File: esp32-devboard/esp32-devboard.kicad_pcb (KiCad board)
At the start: 2 copper layers, 79.4 x 40.6 mm, 33 parts, among them J1 Conn_01x40, J10 Conn_01x02, J11 Conn_01x02, J12 TPS2065DBVR, J13 Conn_01x01, J14 Conn_01x01, J2 Conn_01x40, J3 USB_B_Micro, J4 RJ12, J5 Barrel_Jack_Switch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

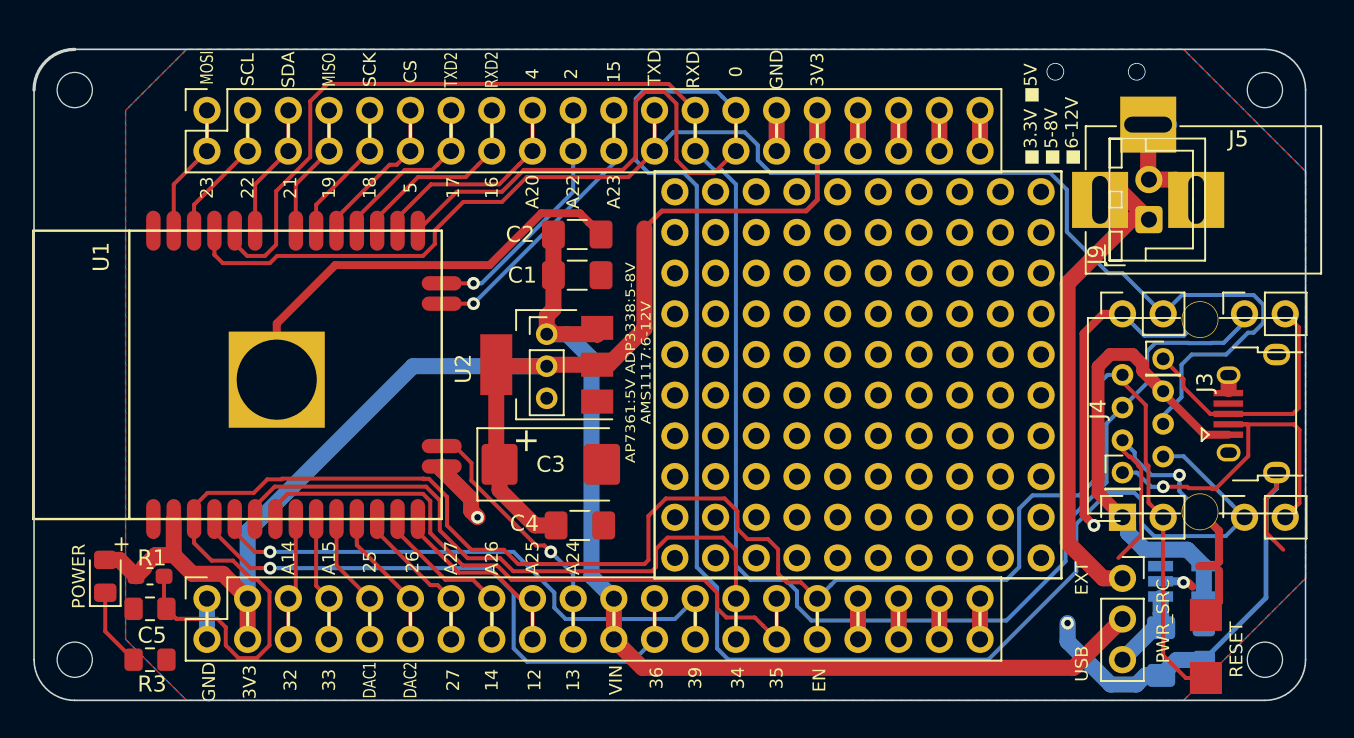
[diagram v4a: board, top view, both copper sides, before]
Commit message: add/enlarge holes
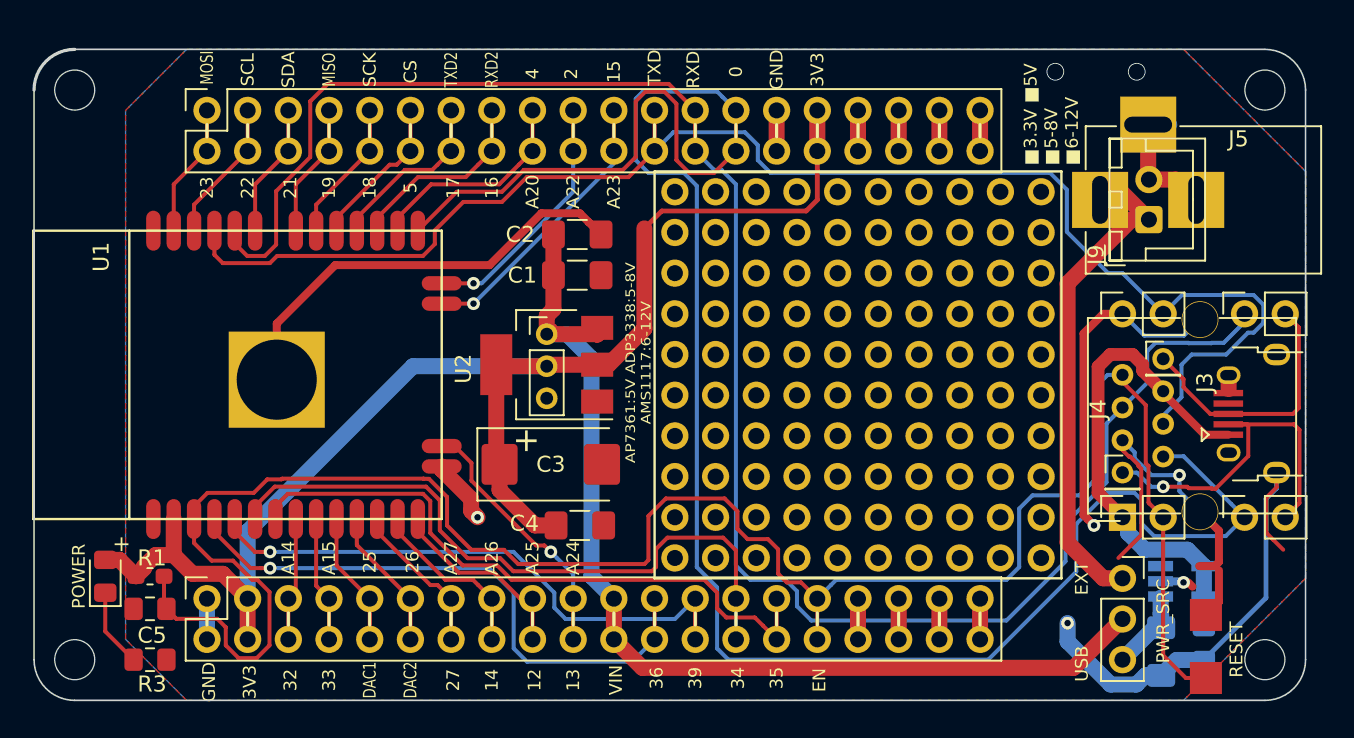
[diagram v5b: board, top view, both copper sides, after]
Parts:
- REF** (x4): value MountingHole_2.2mm_M2 -> MountingHole_2.5mm; footprint MountingHole:MountingHole_2.2mm_M2 -> MountingHole:MountingHole_2.5mm
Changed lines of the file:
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@@
     (add_net GND)
+  )
+  (module MountingHole:MountingHole_2.5mm (layer F.Cu)
+    (at 118.745 110.49)
+    (descr "Mounting Hole 2.5mm, no annular")
+    (tags "mounting hole 2.5mm no annular")
+    (attr virtual)
+    (fp_text reference REF** (at 0 -3.5) (layer F.SilkS) hide
+      (effects (font (size 1 1) (thickness 0.15)))
+    )
+    (fp_text value MountingHole_2.5mm (at 0 3.5) (layer F.Fab)
+      (effects (font (size 1 1) (thickness 0.15)))
+    )
+    (fp_circle (center 0 0) (end 2.75 0) (layer F.CrtYd) (width 0.05))
+    (fp_circle (center 0 0) (end 2.5 0) (layer Cmts.User) (width 0.15))
+    (fp_text user %R (at 0.3 0) (layer F.Fab)
+      (effects (font (size 1 1) (thickness 0.15)))
+    )
+    (pad 1 np_thru_hole circle (at 0 0) (size 2.5 2.5) (drill 2.5) (layers *.Cu *.Mask))
+  )
+  (module MountingHole:MountingHole_2.5mm (layer F.Cu)
+    (at 118.745 74.93)
+    (descr "Mounting Hole 2.5mm, no annular")
+    (tags "mounting hole 2.5mm no annular")
+    (attr virtual)
+    (fp_text reference REF** (at 0 -3.5) (layer F.SilkS) hide
+      (effects (font (size 1 1) (thickness 0.15)))
+    )
+    (fp_text value MountingHole_2.5mm (at 0 3.5) (layer F.Fab)
+      (effects (font (size 1 1) (thickness 0.15)))
+    )
+    (fp_circle (center 0 0) (end 2.75 0) (layer F.CrtYd) (width 0.05))
+    (fp_circle (center 0 0) (end 2.5 0) (layer Cmts.User) (width 0.15))
+    (fp_text user %R (at 0.3 0) (layer F.Fab)
+      (effects (font (size 1 1) (thickness 0.15)))
+    )
+    (pad 1 np_thru_hole circle (at 0 0) (size 2.5 2.5) (drill 2.5) (layers *.Cu *.Mask))
+  )
+  (module MountingHole:MountingHole_2.5mm (layer F.Cu)
+    (at 193.04 110.49)
+    (descr "Mounting Hole 2.5mm, no annular")
+    (tags "mounting hole 2.5mm no annular")
+    (attr virtual)
+    (fp_text reference REF** (at 0 -3.5) (layer F.SilkS) hide
+      (effects (font (size 1 1) (thickness 0.15)))
+    )
+    (fp_text value MountingHole_2.5mm (at 0 3.5) (layer F.Fab)
+      (effects (font (size 1 1) (thickness 0.15)))
+    )
+    (fp_circle (center 0 0) (end 2.75 0) (layer F.CrtYd) (width 0.05))
+    (fp_circle (center 0 0) (end 2.5 0) (layer Cmts.User) (width 0.15))
+    (fp_text user %R (at 0.3 0) (layer F.Fab)
+      (effects (font (size 1 1) (thickness 0.15)))
+    )
+    (pad 1 np_thru_hole circle (at 0 0) (size 2.5 2.5) (drill 2.5) (layers *.Cu *.Mask))
+  )
+  (module MountingHole:MountingHole_2.5mm (layer F.Cu)
+    (at 193.04 74.93)
+    (descr "Mounting Hole 2.5mm, no annular")
+    (tags "mounting hole 2.5mm no annular")
+    (attr virtual)
+    (fp_text reference REF** (at 0 -3.5) (layer F.SilkS) hide
+      (effects (font (size 1 1) (thickness 0.15)))
+    )
+    (fp_text value MountingHole_2.5mm (at 0 3.5) (layer F.Fab)
+      (effects (font (size 1 1) (thickness 0.15)))
+    )
+    (fp_circle (center 0 0) (end 2.75 0) (layer F.CrtYd) (width 0.05))
+    (fp_circle (center 0 0) (end 2.5 0) (layer Cmts.User) (width 0.15))
+    (fp_text user %R (at 0.3 0) (layer F.Fab)
+      (effects (font (size 1 1) (thickness 0.15)))
+    )
+    (pad 1 np_thru_hole circle (at 0 0) (size 2.5 2.5) (drill 2.5) (layers *.Cu *.Mask))
   )
   (module lib:RJ12 (layer F.Cu)
@@
     )
   )
-  (module MountingHole:MountingHole_2.2mm_M2 (layer F.Cu)
-    (at 193.04 110.49)
-    (descr "Mounting Hole 2.2mm, no annular, M2")
-    (tags "mounting hole 2.2mm no annular m2")
-    (attr virtual)
-    (fp_text reference REF** (at 0 -3.2) (layer F.SilkS) hide
-      (effects (font (size 1 1) (thickness 0.15)))
-    )
-    (fp_text value MountingHole_2.2mm_M2 (at 0 3.2) (layer F.Fab)
-      (effects (font (size 1 1) (thickness 0.15)))
-    )
-    (fp_circle (center 0 0) (end 2.45 0) (layer F.CrtYd) (width 0.05))
-    (fp_circle (center 0 0) (end 2.2 0) (layer Cmts.User) (width 0.15))
-    (fp_text user %R (at 0.3 0) (layer F.Fab)
-      (effects (font (size 1 1) (thickness 0.15)))
-    )
-    (pad 1 np_thru_hole circle (at 0 0) (size 2.2 2.2) (drill 2.2) (layers *.Cu *.Mask))
-  )
-  (module MountingHole:MountingHole_2.2mm_M2 (layer F.Cu)
-    (at 193.04 74.93)
-    (descr "Mounting Hole 2.2mm, no annular, M2")
-    (tags "mounting hole 2.2mm no annular m2")
-    (attr virtual)
-    (fp_text reference REF** (at 0 -3.2) (layer F.SilkS) hide
-      (effects (font (size 1 1) (thickness 0.15)))
-    )
-    (fp_text value MountingHole_2.2mm_M2 (at 0 3.2) (layer F.Fab)
-      (effects (font (size 1 1) (thickness 0.15)))
-    )
-    (fp_circle (center 0 0) (end 2.45 0) (layer F.CrtYd) (width 0.05))
-    (fp_circle (center 0 0) (end 2.2 0) (layer Cmts.User) (width 0.15))
-    (fp_text user %R (at 0.3 0) (layer F.Fab)
-      (effects (font (size 1 1) (thickness 0.15)))
-    )
-    (pad 1 np_thru_hole circle (at 0 0) (size 2.2 2.2) (drill 2.2) (layers *.Cu *.Mask))
-  )
   (module Connector_PinSocket_2.54mm:PinSocket_2x20_P2.54mm_Vertical (layer F.Cu)
     (at 127 106.68 90)
@@
     )
   )
-  (module MountingHole:MountingHole_2.2mm_M2 (layer F.Cu)
-    (at 118.745 74.93)
-    (descr "Mounting Hole 2.2mm, no annular, M2")
-    (tags "mounting hole 2.2mm no annular m2")
-    (attr virtual)
-    (fp_text reference REF** (at 0 -3.2) (layer F.SilkS) hide
-      (effects (font (size 1 1) (thickness 0.15)))
-    )
-    (fp_text value MountingHole_2.2mm_M2 (at 0 3.2) (layer F.Fab)
-      (effects (font (size 1 1) (thickness 0.15)))
-    )
-    (fp_circle (center 0 0) (end 2.45 0) (layer F.CrtYd) (width 0.05))
-    (fp_circle (center 0 0) (end 2.2 0) (layer Cmts.User) (width 0.15))
-    (fp_text user %R (at 0.3 0) (layer F.Fab)
-      (effects (font (size 1 1) (thickness 0.15)))
-    )
-    (pad 1 np_thru_hole circle (at 0 0) (size 2.2 2.2) (drill 2.2) (layers *.Cu *.Mask))
-  )
-  (module MountingHole:MountingHole_2.2mm_M2 (layer F.Cu)
-    (at 118.745 110.49)
-    (descr "Mounting Hole 2.2mm, no annular, M2")
-    (tags "mounting hole 2.2mm no annular m2")
-    (attr virtual)
-    (fp_text reference REF** (at 0 -3.2) (layer F.SilkS) hide
-      (effects (font (size 1 1) (thickness 0.15)))
-    )
-    (fp_text value MountingHole_2.2mm_M2 (at 0 3.2) (layer F.Fab)
-      (effects (font (size 1 1) (thickness 0.15)))
-    )
-    (fp_circle (center 0 0) (end 2.45 0) (layer F.CrtYd) (width 0.05))
-    (fp_circle (center 0 0) (end 2.2 0) (layer Cmts.User) (width 0.15))
-    (fp_text user %R (at 0.3 0) (layer F.Fab)
-      (effects (font (size 1 1) (thickness 0.15)))
-    )
-    (pad 1 np_thru_hole circle (at 0 0) (size 2.2 2.2) (drill 2.2) (layers *.Cu *.Mask))
-  )
   (module Connectors:BARREL_JACK (layer F.Cu)
     (at 182.753 81.788 180)
@@
   (segment (start 167.64 106.68) (end 167.64 109.22) (width 1) (layer F.Cu) (net 1))
   (segment (start 170.18 106.68) (end 170.18 109.22) (width 1) (layer F.Cu) (net 2))
-  (segment (start 165.1 76.2) (end 165.1 78.74) (width 1) (layer F.Cu) (net 6))
   (segment (start 167.64 76.2) (end 167.64 78.74) (width 1) (layer F.Cu) (net 3))
   (via (at 179.959 73.787) (size 1.1) (drill 1) (layers F.Cu B.Cu) (net 5))
@@
   (segment (start 143.491001 101.200001) (end 143.491001 100.461741) (width 1) (layer F.Cu) (net 5))
   (segment (start 143.891 101.6) (end 143.491001 101.200001) (width 1) (layer F.Cu) (net 5))
+  (segment (start 165.1 76.2) (end 165.1 78.74) (width 1) (layer F.Cu) (net 6))
   (segment (start 148.114 92.075) (end 148.209 92.17) (width 0.5) (layer F.Cu) (net 6))
   (segment (start 151.264 92.17) (end 151.359 92.075) (width 0.5) (layer F.Cu) (net 6))

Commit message: ESP32-WROVER support
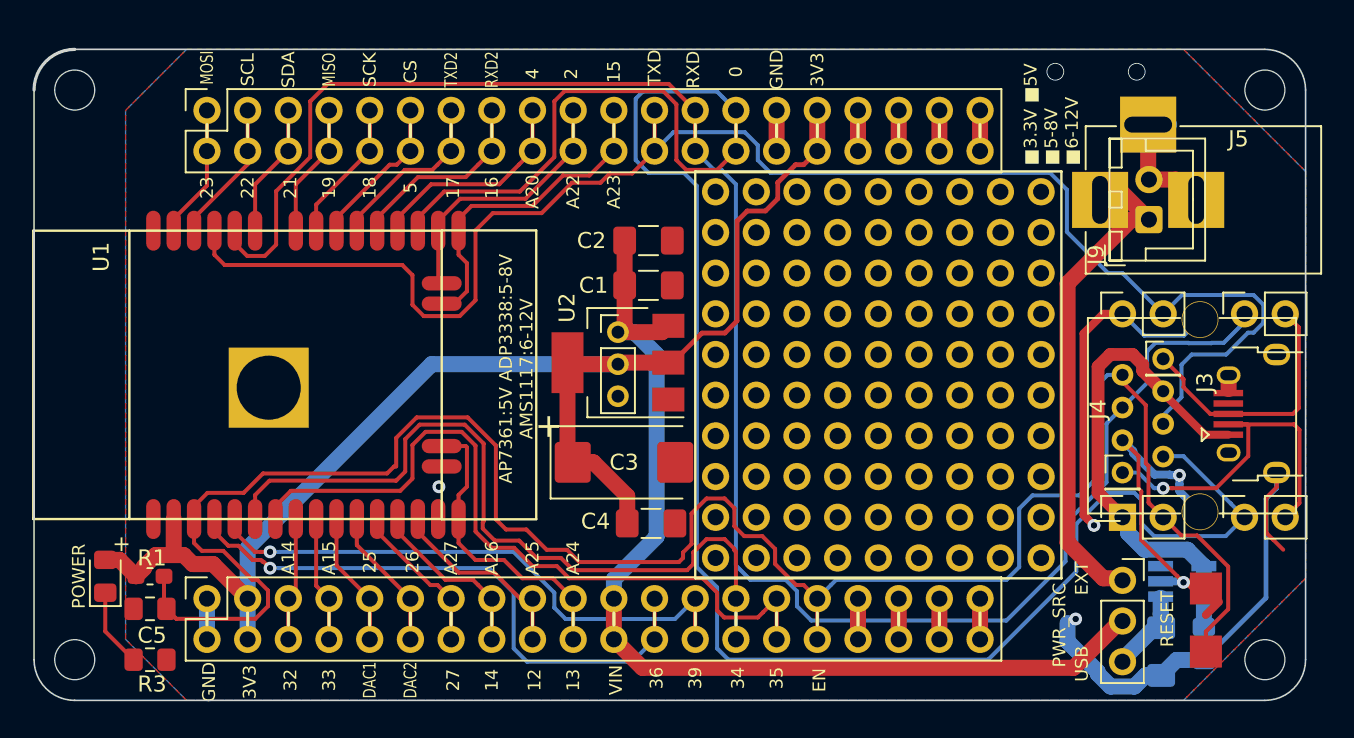
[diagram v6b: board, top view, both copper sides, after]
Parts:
- JX: footprint lib:Prototype_Area_2.54mm_10x10 -> lib:Prototype_Area_2.54mm_09x10
- U1: value ESP32-WROOM -> ESP32-WROOM-WROVER; footprint lib:ESP32-WROOM -> lib:ESP32-WROOM-WROVER
- moved C3 4.57 mm to (153.0, 98.2)
- moved C1 4.49 mm to (154.6, 87.1)
- moved C2 4.46 mm to (154.6, 84.3)
- moved C4 4.45 mm to (154.7, 102.0)
- moved J8 4.45 mm to (152.7, 90.0)
- moved U2 4.45 mm to (152.7, 91.9)
- moved SW1 1.65 mm to (189.4, 108.1)
- moved SW2 0.13 mm to (184.2, 105.5)
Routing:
- net GND: track 122.8 -> 86.7 mm
- net /34: track 42.0 -> 48.5 mm
- net /35: track 40.5 -> 46.9 mm
- net /TXD: track 92.6 -> 98.5 mm
- net /IO15: track 17.7 -> 20.6 mm, vias 1 -> 0
- net /IO13: track 16.2 -> 18.9 mm, vias 1 -> 0
- net /3V3: track 89.2 -> 86.8 mm
- net /VIN: track 66.4 -> 64.4 mm
- net /IO2: track 15.7 -> 16.8 mm, vias 1 -> 0
